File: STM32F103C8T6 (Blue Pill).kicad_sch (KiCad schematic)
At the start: 30 parts, among them J1 Conn_02x03_Odd_Even, J2 USB_B_Micro, J3 Conn_01x04_Socket, U4 RT9193-33GB, U5 STM32F103C8T6, Y1 8MHz, Y2 32.768Khz

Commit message: Schematic Almost Completed and PCB Tracing going on
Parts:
- C20, C21, C22, C23, C24, C25, C26, C27, C28, C29, C30, C31, C32, C33, C7: footprint (none) -> Capacitor_SMD:C_0603_1608Metric
- J1: footprint Connector_PinHeader_2.54mm:PinHeader_2x03_P2.54mm_Vertical -> Connector_PinHeader_2.54mm:PinHeader_2x03_P2.54mm_Vertical_SMD
- J2: footprint (none) -> Connector_USB:USB_Micro-B_Wuerth_629105150521
- J3: footprint (none) -> Connector_PinSocket_2.54mm:PinSocket_1x04_P2.54mm_Horizontal
- R12, R13, R14, R15, R16, R17, R5: footprint (none) -> Resistor_SMD:R_1206_3216Metric
- Y1, Y2: footprint (none) -> Crystal:Crystal_SMD_3215-2Pin_3.2x1.5mm
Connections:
- net 5V: no longer U4.1 (VIN), U4.3 (EN)
- net GND: no longer U4.2 (GND)
- net VCC3V3: no longer U4.5 (VOUT)
- net at U4.4 (BP): no longer C22.1
- net at U5.23 (VSS): now also U5.35 (VSS), U5.47 (VSS)
- net at U5.24 (VDD): now also U5.36 (VDD), U5.48 (VDD)
- no-connect marks 0 -> 29
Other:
- title: (none) -> {HIGH_POWER_CONTROL_UNIT}
- moved on the sheet: R14, R15, U4

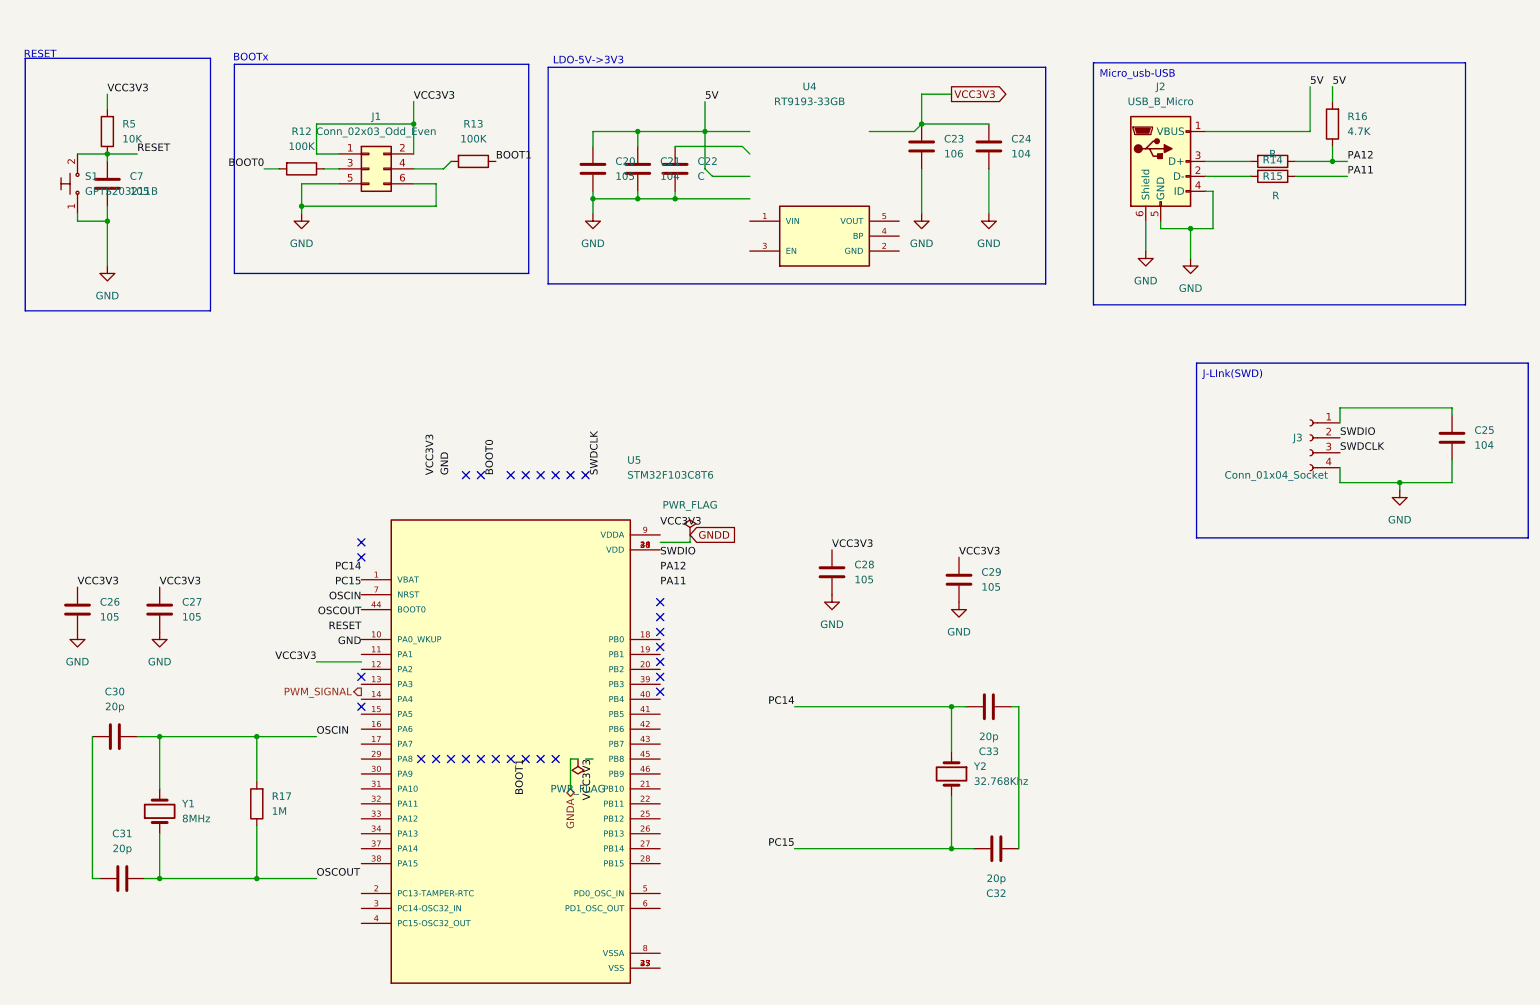
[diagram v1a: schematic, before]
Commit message: Added .gitignore to prevent ZIP files from being tracked
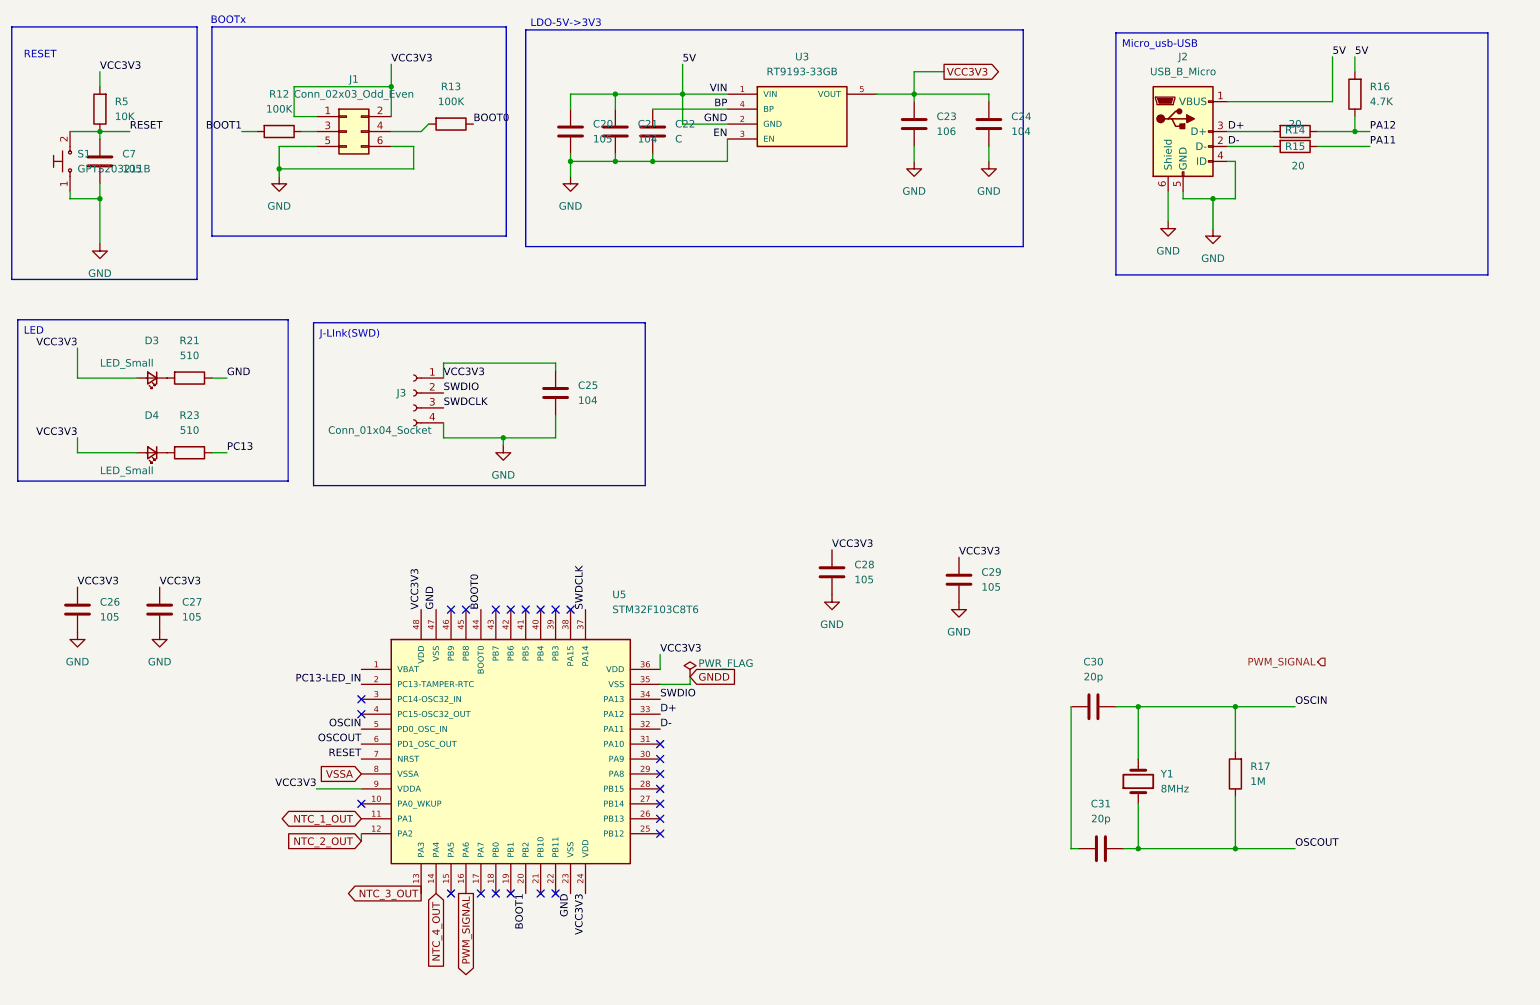
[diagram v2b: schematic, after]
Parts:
- removed C32, C33: 20p, Capacitor_SMD:C_0603_1608Metric, symbol Device:C
- removed U4: RT9193-33GB, RT9193-33GB:SOT94P279X129-5N, symbol RT9193-33GB:RT9193-33GB
- removed Y2: 32.768Khz, Crystal:Crystal_SMD_3215-2Pin_3.2x1.5mm, symbol Device:Crystal
- added D3, D4: LED_Small, LED_SMD:LED_0603_1608Metric_Pad1.05x0.95mm_HandSolder, symbol Device:LED_Small
- added R21, R23: 510, Resistor_SMD:R_1206_3216Metric, symbol Device:R
- added U3: RT9193-33GB, RT9193-33GB:SOT94P279X129-5N, symbol RT9193-33GB:RT9193-33GB
- R14, R15: value R -> 20
- S1: footprint digikey-footprints:PushButton_12x12mm_THT_GPTS203211B -> Button_Switch_SMD:SW_SPST_B3U-1000P
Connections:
- net 5V is gone; now on net GND: C20.1, C21.1, J2.1 (VBUS), R16.2
- net BOOT0: now also R13.1, U5.44 (BOOT0); no longer R12.2
- net BOOT1: now also R12.2, U5.20 (PB2); no longer R13.1
- net GND: now also U5.23 (VSS), U5.47 (VSS), R21.1, U3.1 (VIN), U3.2 (GND), U3.3 (EN)
- net GNDD: now also U5.35 (VSS)
- net OSCIN: now also U5.5 (PD0_OSC_IN)
- net OSCOUT: now also U5.6 (PD1_OSC_OUT)
- net PWM_SIGNAL: now also U5.16 (PA6)
- net RESET: now also U5.7 (NRST)
- net SWDCLK: now also U5.37 (PA14)
- net SWDIO: now also U5.34 (PA13)
- net VCC3V3: now also C25.1, J3.1 (Pin_1), U5.24 (VDD), U5.36 (VDD), U5.48 (VDD), U5.9 (VDDA), D3.2 (A), D4.2 (A), U3.5 (VOUT)
- net BP: now reaches C22.1
- net BP: now also U3.4 (BP)
- net D+: now reaches J2.3 (D+), R14.2
- net D+: now also U5.33 (PA12)
- net D-: now reaches J2.2 (D-), R15.2
- net D-: now also U5.32 (PA11)
- net NTC_1_OUT: now reaches U5.11 (PA1)
- net NTC_2_OUT: now reaches U5.12 (PA2)
- net NTC_3_OUT: now reaches U5.13 (PA3)
- net NTC_4_OUT: now reaches U5.14 (PA4)
- net PC13-LED_IN: now reaches U5.2 (PC13-TAMPER-RTC)
- net VSSA: now reaches U5.8 (VSSA)
- new net: D3.1 (K), R21.2
- new net: D4.1 (K), R23.2
- new net PC13: R23.1
- no-connect marks 29 -> 24
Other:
- moved on the sheet: C20, C21, C22, C23, C24, C25, C30, C31, C7, J1, J2, J3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
